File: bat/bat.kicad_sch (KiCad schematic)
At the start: 23 parts, among them J1 Conn_01x02_Pin, J10 Conn_01x05_Socket, J2 Conn_01x02_Pin, J3 Conn_01x02_Pin, J4 Conn_01x02_Pin, J6 USB_C_Receptacle_PowerOnly_6P, J7 Conn_01x05_Socket, J8 Conn_01x05_Socket, J9 Conn_01x05_Socket, Q1 BC02P28TA, U1 MICRONE ME2801A33M3G, U2 BQ2404

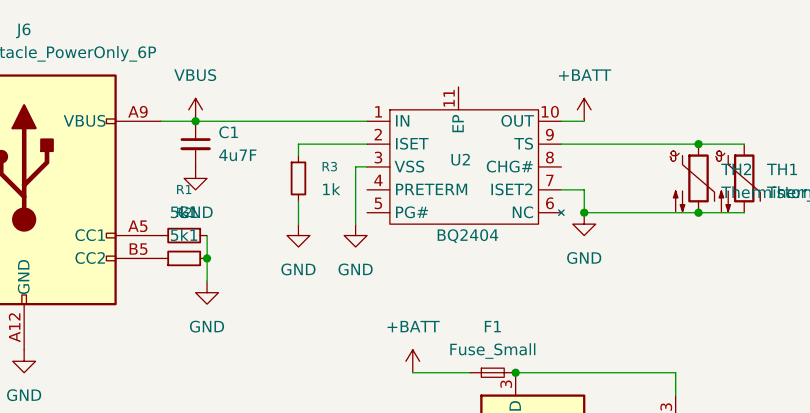
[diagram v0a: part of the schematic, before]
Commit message: fixed BQ24040DSQR layout to be 2x2mm in stead of 2.5, also added heat pad after actually reading datasheet lol
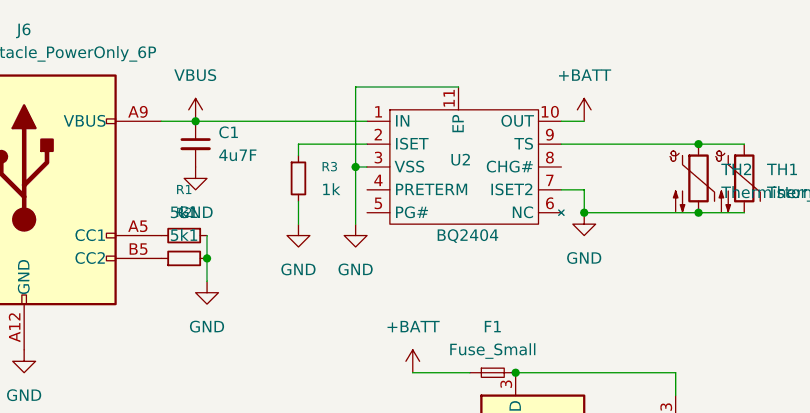
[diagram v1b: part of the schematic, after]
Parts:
- U2: footprint Package_SON:WSON-10-1EP_2.5x2.5mm_P0.5mm_EP1.2x2mm_ThermalVias -> Package_DFN_QFN:Texas_DLH0010A_WSON-10-1EP_2.2x2mm_P0.4mm_EP0.9x1.5mm_ThermalVias
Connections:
- net GND: now also U2.11 (EP)
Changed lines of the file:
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@@
 		(color 0 0 0 0)
 	)
+	(junction
+		(at 66.04 80.01)
+		(diameter 0)
+		(color 0 0 0 0)
+	)
 	(wire
 		(pts
@@
 		(pts
 			(xy 119.38 119.38) (xy 129.54 119.38)
+		)
+		(stroke
+			(width 0)
+			(type default)
+		)
+	)
+	(wire
+		(pts
+			(xy 77.47 71.12) (xy 66.04 71.12)
+		)
+		(stroke
+			(width 0)
+			(type default)
+		)
+	)
+	(wire
+		(pts
+			(xy 66.04 71.12) (xy 66.04 80.01)
 		)
 		(stroke
@@
 			)
 		)
-		(property "Footprint" "Package_SON:WSON-10-1EP_2.5x2.5mm_P0.5mm_EP1.2x2mm_ThermalVias"
+		(property "Footprint" "Package_DFN_QFN:Texas_DLH0010A_WSON-10-1EP_2.2x2mm_P0.4mm_EP0.9x1.5mm_ThermalVias"
 			(at 72.39 77.47 0)
 			(effects
